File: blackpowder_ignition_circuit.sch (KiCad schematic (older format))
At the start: 6 parts, among them J2 Conn_01x02, Q1 FDS6898A

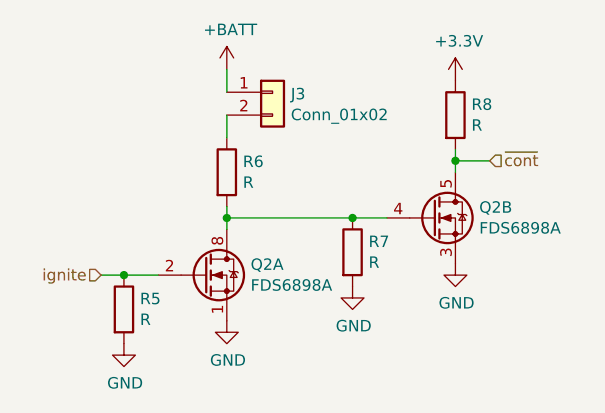
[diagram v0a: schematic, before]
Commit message: removed circuits that can't be fit in
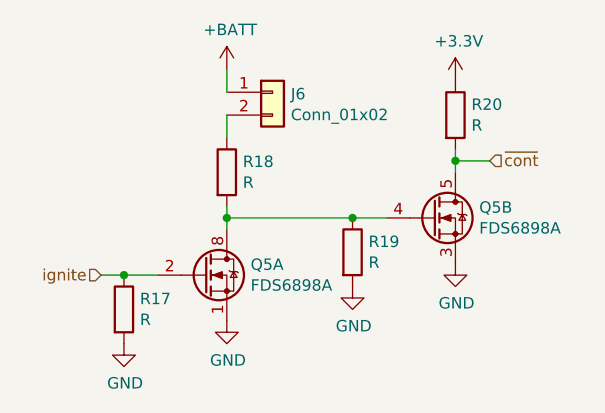
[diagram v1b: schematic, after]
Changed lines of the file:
@@
 $Descr A4 11693 8268
 encoding utf-8
-Sheet 2 8
+Sheet 5 6
 Title ""
 Date ""
@@
 AR Path="/5EB223EE/5EAFF725" Ref="Q7"  Part="1"
 AR Path="/5EB223F2/5EAFF725" Ref="Q8"  Part="1"
-F 0 "Q2" H 4404 4046 50  0000 L CNN
+F 0 "Q5" H 4404 4046 50  0000 L CNN
 F 1 "FDS6898A" H 4404 3955 50  0000 L CNN
 F 2 "Package_SO:SOIC-8_3.9x4.9mm_P1.27mm" H 4400 3925 50  0001 L CIN
@@
 AR Path="/5EB223EE/5EAFF72B" Ref="R25"  Part="1"
 AR Path="/5EB223F2/5EAFF72B" Ref="R29"  Part="1"
-F 0 "R5" H 3920 4196 50  0000 L CNN
+F 0 "R17" H 3920 4196 50  0000 L CNN
 F 1 "R" H 3920 4105 50  0000 L CNN
 F 2 "Resistor_SMD:R_0603_1608Metric_Pad1.05x0.95mm_HandSolder" V 3780 4150 50  0001 C CNN
@@
 AR Path="/5EB223EE/5EAFF731" Ref="R26"  Part="1"
 AR Path="/5EB223F2/5EAFF731" Ref="R30"  Part="1"
-F 0 "R6" H 4370 3596 50  0000 L CNN
+F 0 "R18" H 4370 3596 50  0000 L CNN
 F 1 "R" H 4370 3505 50  0000 L CNN
 F 2 "star-common-lib:PWR163" V 4230 3550 50  0001 C CNN
@@
 AR Path="/5EB223EE/5EAFF737" Ref="R27"  Part="1"
 AR Path="/5EB223F2/5EAFF737" Ref="R31"  Part="1"
-F 0 "R7" H 4920 3946 50  0000 L CNN
+F 0 "R19" H 4920 3946 50  0000 L CNN
 F 1 "R" H 4920 3855 50  0000 L CNN
 F 2 "Resistor_SMD:R_0603_1608Metric_Pad1.05x0.95mm_HandSolder" V 4780 3900 50  0001 C CNN
@@
 AR Path="/5EB223EE/5EAFF73D" Ref="Q7"  Part="2"
 AR Path="/5EB223F2/5EAFF73D" Ref="Q8"  Part="2"
-F 0 "Q2" H 5404 3796 50  0000 L CNN
+F 0 "Q5" H 5404 3796 50  0000 L CNN
 F 1 "FDS6898A" H 5404 3705 50  0000 L CNN
 F 2 "Package_SO:SOIC-8_3.9x4.9mm_P1.27mm" H 5400 3675 50  0001 L CIN
@@
 AR Path="/5EB223EE/5EAFF743" Ref="R28"  Part="1"
 AR Path="/5EB223F2/5EAFF743" Ref="R32"  Part="1"
-F 0 "R8" H 5370 3346 50  0000 L CNN
+F 0 "R20" H 5370 3346 50  0000 L CNN
 F 1 "R" H 5370 3255 50  0000 L CNN
 F 2 "Resistor_SMD:R_0603_1608Metric_Pad1.05x0.95mm_HandSolder" V 5230 3300 50  0001 C CNN
@@
 AR Path="/5EB223EE/5EAFF758" Ref="#PWR0137"  Part="1"
 AR Path="/5EB223F2/5EAFF758" Ref="#PWR0143"  Part="1"
-F 0 "#PWR0101" H 3850 4050 50  0001 C CNN
+F 0 "#PWR0125" H 3850 4050 50  0001 C CNN
 F 1 "GND" H 3855 4127 50  0000 C CNN
 F 2 "" H 3850 4300 50  0001 C CNN
@@
 AR Path="/5EB223EE/5EAFF75E" Ref="#PWR0138"  Part="1"
 AR Path="/5EB223F2/5EAFF75E" Ref="#PWR0144"  Part="1"
-F 0 "#PWR0102" H 4300 3950 50  0001 C CNN
+F 0 "#PWR0126" H 4300 3950 50  0001 C CNN
 F 1 "GND" H 4305 4027 50  0000 C CNN
 F 2 "" H 4300 4200 50  0001 C CNN
@@
 AR Path="/5EB223EE/5EAFF764" Ref="#PWR0139"  Part="1"
 AR Path="/5EB223F2/5EAFF764" Ref="#PWR0145"  Part="1"
-F 0 "#PWR0103" H 5300 3700 50  0001 C CNN
+F 0 "#PWR0127" H 5300 3700 50  0001 C CNN
 F 1 "GND" H 5305 3777 50  0000 C CNN
 F 2 "" H 5300 3950 50  0001 C CNN
@@
 AR Path="/5EB223EE/5EAFF76A" Ref="#PWR0140"  Part="1"
 AR Path="/5EB223F2/5EAFF76A" Ref="#PWR0146"  Part="1"
-F 0 "#PWR0104" H 4850 3800 50  0001 C CNN
+F 0 "#PWR0128" H 4850 3800 50  0001 C CNN
 F 1 "GND" H 4855 3877 50  0000 C CNN
 F 2 "" H 4850 4050 50  0001 C CNN
@@
 AR Path="/5EB223EE/5EAFF770" Ref="#PWR0141"  Part="1"
 AR Path="/5EB223F2/5EAFF770" Ref="#PWR0147"  Part="1"
-F 0 "#PWR0105" H 5300 3000 50  0001 C CNN
+F 0 "#PWR0129" H 5300 3000 50  0001 C CNN
 F 1 "+3.3V" H 5315 3323 50  0000 C CNN
 F 2 "" H 5300 3150 50  0001 C CNN
@@
 AR Path="/5EB223EE/5EAFF776" Ref="#PWR0142"  Part="1"
 AR Path="/5EB223F2/5EAFF776" Ref="#PWR0148"  Part="1"
-F 0 "#PWR0106" H 4300 2950 50  0001 C CNN
+F 0 "#PWR0130" H 4300 2950 50  0001 C CNN
 F 1 "+BATT" H 4315 3273 50  0000 C CNN
 F 2 "" H 4300 3100 50  0001 C CNN
@@
 AR Path="/5EB223EE/5EAFF77D" Ref="J8"  Part="1"
 AR Path="/5EB223F2/5EAFF77D" Ref="J9"  Part="1"
-F 0 "J3" H 4580 3192 50  0000 L CNN
+F 0 "J6" H 4580 3192 50  0000 L CNN
 F 1 "Conn_01x02" H 4580 3101 50  0000 L CNN
 F 2 "Connector_Molex:Molex_Mini-Fit_Jr_5569-02A2_2x01_P4.20mm_Horizontal" H 4500 3200 50  0001 C CNN

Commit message: everything hooked up, cleaned layout up, silkscreen
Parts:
- removed R2: R, star-common-lib:PWR163, symbol Device:R
- added J9: Conn_01x03, star-common-lib:PWR163, symbol Connector_Generic:Conn_01x03
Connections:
- wire segments 11 -> 12
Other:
- note added: "Resistor, pin 2 is heatsink"
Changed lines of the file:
@@
 $Descr A4 11693 8268
 encoding utf-8
-Sheet 5 6
+Sheet 5 5
 Title ""
 Date ""
@@
 AR Path="/5EB223EE/5EAFF725" Ref="Q7"  Part="1"
 AR Path="/5EB223F2/5EAFF725" Ref="Q8"  Part="1"
-F 0 "Q5" H 4404 4046 50  0000 L CNN
+F 0 "Q1" H 4404 4046 50  0000 L CNN
 F 1 "FDS6898A" H 4404 3955 50  0000 L CNN
 F 2 "Package_SO:SOIC-8_3.9x4.9mm_P1.27mm" H 4400 3925 50  0001 L CIN
@@
 AR Path="/5EB223EE/5EAFF72B" Ref="R25"  Part="1"
 AR Path="/5EB223F2/5EAFF72B" Ref="R29"  Part="1"
-F 0 "R17" H 3920 4196 50  0000 L CNN
+F 0 "R1" H 3920 4196 50  0000 L CNN
 F 1 "R" H 3920 4105 50  0000 L CNN
 F 2 "Resistor_SMD:R_0603_1608Metric_Pad1.05x0.95mm_HandSolder" V 3780 4150 50  0001 C CNN
 F 3 "~" H 3850 4150 50  0001 C CNN
 	1    3850 4150
-	1    0    0    -1
-$EndComp
-$Comp
-L Device:R R?
-U 1 1 5EAFF731
-P 4300 3550
-AR Path="/5EAFF731" Ref="R?"  Part="1"
-AR Path="/5EAF9C8B/5EAFF731" Ref="R2"  Part="1"
-AR Path="/5EB11141/5EAFF731" Ref="R?"  Part="1"
-AR Path="/5EB1278B/5EAFF731" Ref="R6"  Part="1"
-AR Path="/5EB12B7D/5EAFF731" Ref="R10"  Part="1"
-AR Path="/5EB12D6D/5EAFF731" Ref="R14"  Part="1"
-AR Path="/5EB1EA7C/5EAFF731" Ref="R18"  Part="1"
-AR Path="/5EB223E6/5EAFF731" Ref="R18"  Part="1"
-AR Path="/5EB223EA/5EAFF731" Ref="R22"  Part="1"
-AR Path="/5EB223EE/5EAFF731" Ref="R26"  Part="1"
-AR Path="/5EB223F2/5EAFF731" Ref="R30"  Part="1"
-F 0 "R18" H 4370 3596 50  0000 L CNN
-F 1 "R" H 4370 3505 50  0000 L CNN
-F 2 "star-common-lib:PWR163" V 4230 3550 50  0001 C CNN
-F 3 "~" H 4300 3550 50  0001 C CNN
-	1    4300 3550
 	1    0    0    -1
 $EndComp
@@
 AR Path="/5EB223EE/5EAFF737" Ref="R27"  Part="1"
 AR Path="/5EB223F2/5EAFF737" Ref="R31"  Part="1"
-F 0 "R19" H 4920 3946 50  0000 L CNN
+F 0 "R3" H 4920 3946 50  0000 L CNN
 F 1 "R" H 4920 3855 50  0000 L CNN
 F 2 "Resistor_SMD:R_0603_1608Metric_Pad1.05x0.95mm_HandSolder" V 4780 3900 50  0001 C CNN
@@
 AR Path="/5EB223EE/5EAFF73D" Ref="Q7"  Part="2"
 AR Path="/5EB223F2/5EAFF73D" Ref="Q8"  Part="2"
-F 0 "Q5" H 5404 3796 50  0000 L CNN
+F 0 "Q1" H 5404 3796 50  0000 L CNN
 F 1 "FDS6898A" H 5404 3705 50  0000 L CNN
 F 2 "Package_SO:SOIC-8_3.9x4.9mm_P1.27mm" H 5400 3675 50  0001 L CIN
@@
 AR Path="/5EB223EE/5EAFF743" Ref="R28"  Part="1"
 AR Path="/5EB223F2/5EAFF743" Ref="R32"  Part="1"
-F 0 "R20" H 5370 3346 50  0000 L CNN
+F 0 "R4" H 5370 3346 50  0000 L CNN
 F 1 "R" H 5370 3255 50  0000 L CNN
 F 2 "Resistor_SMD:R_0603_1608Metric_Pad1.05x0.95mm_HandSolder" V 5230 3300 50  0001 C CNN
@@
 Wire Wire Line
 	4850 3750 4300 3750
-Wire Wire Line
-	4300 3700 4300 3750
 Connection ~ 4850 3750
 Connection ~ 4300 3750
@@
 AR Path="/5EB223EE/5EAFF758" Ref="#PWR0137"  Part="1"
 AR Path="/5EB223F2/5EAFF758" Ref="#PWR0143"  Part="1"
-F 0 "#PWR0125" H 3850 4050 50  0001 C CNN
+F 0 "#PWR0101" H 3850 4050 50  0001 C CNN
 F 1 "GND" H 3855 4127 50  0000 C CNN
 F 2 "" H 3850 4300 50  0001 C CNN
@@
 AR Path="/5EB223EE/5EAFF75E" Ref="#PWR0138"  Part="1"
 AR Path="/5EB223F2/5EAFF75E" Ref="#PWR0144"  Part="1"
-F 0 "#PWR0126" H 4300 3950 50  0001 C CNN
+F 0 "#PWR0102" H 4300 3950 50  0001 C CNN
 F 1 "GND" H 4305 4027 50  0000 C CNN
 F 2 "" H 4300 4200 50  0001 C CNN
@@
 AR Path="/5EB223EE/5EAFF764" Ref="#PWR0139"  Part="1"
 AR Path="/5EB223F2/5EAFF764" Ref="#PWR0145"  Part="1"
-F 0 "#PWR0127" H 5300 3700 50  0001 C CNN
+F 0 "#PWR0103" H 5300 3700 50  0001 C CNN
 F 1 "GND" H 5305 3777 50  0000 C CNN
 F 2 "" H 5300 3950 50  0001 C CNN
@@
 AR Path="/5EB223EE/5EAFF76A" Ref="#PWR0140"  Part="1"
 AR Path="/5EB223F2/5EAFF76A" Ref="#PWR0146"  Part="1"
-F 0 "#PWR0128" H 4850 3800 50  0001 C CNN
+F 0 "#PWR0104" H 4850 3800 50  0001 C CNN
 F 1 "GND" H 4855 3877 50  0000 C CNN
 F 2 "" H 4850 4050 50  0001 C CNN
@@
 AR Path="/5EB223EE/5EAFF770" Ref="#PWR0141"  Part="1"
 AR Path="/5EB223F2/5EAFF770" Ref="#PWR0147"  Part="1"
-F 0 "#PWR0129" H 5300 3000 50  0001 C CNN
+F 0 "#PWR0105" H 5300 3000 50  0001 C CNN
 F 1 "+3.3V" H 5315 3323 50  0000 C CNN
 F 2 "" H 5300 3150 50  0001 C CNN
@@
 AR Path="/5EB223EE/5EAFF776" Ref="#PWR0142"  Part="1"
 AR Path="/5EB223F2/5EAFF776" Ref="#PWR0148"  Part="1"
-F 0 "#PWR0130" H 4300 2950 50  0001 C CNN
+F 0 "#PWR0106" H 4300 2950 50  0001 C CNN
 F 1 "+BATT" H 4315 3273 50  0000 C CNN
 F 2 "" H 4300 3100 50  0001 C CNN
@@
 	1    0    0    -1
 $EndComp
-Wire Wire Line
-	4300 3400 4300 3300
 $Comp
 L Connector_Generic:Conn_01x02 J?
@@
 AR Path="/5EB223EE/5EAFF77D" Ref="J8"  Part="1"
 AR Path="/5EB223F2/5EAFF77D" Ref="J9"  Part="1"
-F 0 "J6" H 4580 3192 50  0000 L CNN
+F 0 "J2" H 4580 3192 50  0000 L CNN
 F 1 "Conn_01x02" H 4580 3101 50  0000 L CNN
 F 2 "Connector_Molex:Molex_Mini-Fit_Jr_5569-02A2_2x01_P4.20mm_Horizontal" H 4500 3200 50  0001 C CNN
@@
 Text HLabel 5450 3500 2    50   Input ~ 0
 ~cont~
+$Comp
+L Connector_Generic:Conn_01x03 J9
+U 1 1 5EF99B5F
+P 4500 3550
+AR Path="/5EB12D6D/5EF99B5F" Ref="J9"  Part="1"
+AR Path="/5EB1278B/5EF99B5F" Ref="J6"  Part="1"
+AR Path="/5EB12B7D/5EF99B5F" Ref="J7"  Part="1"
+AR Path="/5EAF9C8B/5EF99B5F" Ref="J10"  Part="1"
+F 0 "J10" H 4580 3592 50  0000 L CNN
+F 1 "Conn_01x03" H 4580 3501 50  0000 L CNN
+F 2 "star-common-lib:PWR163" H 4500 3550 50  0001 C CNN
+F 3 "~" H 4500 3550 50  0001 C CNN
+	1    4500 3550
+	1    0    0    -1
+$EndComp
+Wire Wire Line
+	4300 3650 4300 3750
+Wire Wire Line
+	4300 3300 4300 3450
+$Comp
+L power:GND #PWR?
+U 1 1 5EF9AB74
+P 4100 3550
+AR Path="/5EF9AB74" Ref="#PWR?"  Part="1"
+AR Path="/5EAF9C8B/5EF9AB74" Ref="#PWR010"  Part="1"
+AR Path="/5EB11141/5EF9AB74" Ref="#PWR?"  Part="1"
+AR Path="/5EB1278B/5EF9AB74" Ref="#PWR07"  Part="1"
+AR Path="/5EB12B7D/5EF9AB74" Ref="#PWR08"  Part="1"
+AR Path="/5EB12D6D/5EF9AB74" Ref="#PWR09"  Part="1"
+AR Path="/5EB1EA7C/5EF9AB74" Ref="#PWR?"  Part="1"
+AR Path="/5EB223E6/5EF9AB74" Ref="#PWR?"  Part="1"
+AR Path="/5EB223EA/5EF9AB74" Ref="#PWR?"  Part="1"
+AR Path="/5EB223EE/5EF9AB74" Ref="#PWR?"  Part="1"
+AR Path="/5EB223F2/5EF9AB74" Ref="#PWR?"  Part="1"
+F 0 "#PWR010" H 4100 3300 50  0001 C CNN
+F 1 "GND" H 4105 3377 50  0000 C CNN
+F 2 "" H 4100 3550 50  0001 C CNN
+F 3 "" H 4100 3550 50  0001 C CNN
+	1    4100 3550
+	1    0    0    -1
+$EndComp
+Wire Wire Line
+	4100 3550 4300 3550
+Text Notes 2950 3550 0    50   ~ 0
+Resistor, pin 2 is heatsink
 $EndSCHEMATC

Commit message: most functionality
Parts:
- removed J9: Conn_01x03, star-common-lib:PWR163, symbol Connector_Generic:Conn_01x03
- added R6: 3R, star-common-lib:PWR163, symbol star-common-lib:R_Heatsink
- J2: footprint Connector_Molex:Molex_Mini-Fit_Jr_5569-02A2_2x01_P4.20mm_Horizontal -> star-common-lib:Molex_Mini-Fit_Jr_5569-02A2_2x01_P4.20mm_Horizontal
- R1, R3: value R -> 100k
- R4: value R -> 50k
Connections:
- wire segments 12 -> 10
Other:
- note removed: "Resistor, pin 2 is heatsink"
- moved on the sheet: R4
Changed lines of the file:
@@
 $Descr A4 11693 8268
 encoding utf-8
-Sheet 5 5
+Sheet 4 5
 Title ""
 Date ""
@@
 AR Path="/5EB223F2/5EAFF72B" Ref="R29"  Part="1"
 F 0 "R1" H 3920 4196 50  0000 L CNN
-F 1 "R" H 3920 4105 50  0000 L CNN
+F 1 "100k" H 3920 4105 50  0000 L CNN
 F 2 "Resistor_SMD:R_0603_1608Metric_Pad1.05x0.95mm_HandSolder" V 3780 4150 50  0001 C CNN
 F 3 "~" H 3850 4150 50  0001 C CNN
@@
 AR Path="/5EB223F2/5EAFF737" Ref="R31"  Part="1"
 F 0 "R3" H 4920 3946 50  0000 L CNN
-F 1 "R" H 4920 3855 50  0000 L CNN
+F 1 "100k" H 4920 3855 50  0000 L CNN
 F 2 "Resistor_SMD:R_0603_1608Metric_Pad1.05x0.95mm_HandSolder" V 4780 3900 50  0001 C CNN
 F 3 "~" H 4850 3900 50  0001 C CNN
@@
 L Device:R R?
 U 1 1 5EAFF743
-P 5300 3300
+P 5300 4150
 AR Path="/5EAFF743" Ref="R?"  Part="1"
 AR Path="/5EAF9C8B/5EAFF743" Ref="R4"  Part="1"
@@
 AR Path="/5EB223EE/5EAFF743" Ref="R28"  Part="1"
 AR Path="/5EB223F2/5EAFF743" Ref="R32"  Part="1"
-F 0 "R4" H 5370 3346 50  0000 L CNN
-F 1 "R" H 5370 3255 50  0000 L CNN
-F 2 "Resistor_SMD:R_0603_1608Metric_Pad1.05x0.95mm_HandSolder" V 5230 3300 50  0001 C CNN
-F 3 "~" H 5300 3300 50  0001 C CNN
-	1    5300 3300
+F 0 "R4" H 5370 4196 50  0000 L CNN
+F 1 "50k" H 5370 4105 50  0000 L CNN
+F 2 "Resistor_SMD:R_0603_1608Metric_Pad1.05x0.95mm_HandSolder" V 5230 4150 50  0001 C CNN
+F 3 "~" H 5300 4150 50  0001 C CNN
+	1    5300 4150
 	1    0    0    -1
 $EndComp
@@
 	4300 3750 4300 3800
 Wire Wire Line
-	5300 3450 5300 3500
-Wire Wire Line
 	3750 4000 3850 4000
 Connection ~ 3850 4000
-Wire Wire Line
-	5450 3500 5300 3500
-Connection ~ 5300 3500
-Wire Wire Line
-	5300 3500 5300 3550
 $Comp
 L power:GND #PWR?
@@
 L power:GND #PWR?
 U 1 1 5EAFF764
-P 5300 3950
+P 5300 4300
 AR Path="/5EAFF764" Ref="#PWR?"  Part="1"
 AR Path="/5EAF9C8B/5EAFF764" Ref="#PWR0103"  Part="1"
@@
 AR Path="/5EB223EE/5EAFF764" Ref="#PWR0139"  Part="1"
 AR Path="/5EB223F2/5EAFF764" Ref="#PWR0145"  Part="1"
-F 0 "#PWR0103" H 5300 3700 50  0001 C CNN
-F 1 "GND" H 5305 3777 50  0000 C CNN
-F 2 "" H 5300 3950 50  0001 C CNN
-F 3 "" H 5300 3950 50  0001 C CNN
-	1    5300 3950
+F 0 "#PWR0103" H 5300 4050 50  0001 C CNN
+F 1 "GND" H 5305 4127 50  0000 C CNN
+F 2 "" H 5300 4300 50  0001 C CNN
+F 3 "" H 5300 4300 50  0001 C CNN
+	1    5300 4300
 	1    0    0    -1
 $EndComp
@@
 L power:+3.3V #PWR?
 U 1 1 5EAFF770
-P 5300 3150
+P 5300 3550
 AR Path="/5EAFF770" Ref="#PWR?"  Part="1"
 AR Path="/5EAF9C8B/5EAFF770" Ref="#PWR0105"  Part="1"
@@
 AR Path="/5EB223EE/5EAFF770" Ref="#PWR0141"  Part="1"
 AR Path="/5EB223F2/5EAFF770" Ref="#PWR0147"  Part="1"
-F 0 "#PWR0105" H 5300 3000 50  0001 C CNN
-F 1 "+3.3V" H 5315 3323 50  0000 C CNN
-F 2 "" H 5300 3150 50  0001 C CNN
-F 3 "" H 5300 3150 50  0001 C CNN
-	1    5300 3150
+F 0 "#PWR0105" H 5300 3400 50  0001 C CNN
+F 1 "+3.3V" H 5315 3723 50  0000 C CNN
+F 2 "" H 5300 3550 50  0001 C CNN
+F 3 "" H 5300 3550 50  0001 C CNN
+	1    5300 3550
 	1    0    0    -1
 $EndComp
@@
 F 0 "J2" H 4580 3192 50  0000 L CNN
 F 1 "Conn_01x02" H 4580 3101 50  0000 L CNN
-F 2 "Connector_Molex:Molex_Mini-Fit_Jr_5569-02A2_2x01_P4.20mm_Horizontal" H 4500 3200 50  0001 C CNN
+F 2 "star-common-lib:Molex_Mini-Fit_Jr_5569-02A2_2x01_P4.20mm_Horizontal" H 4500 3200 50  0001 C CNN
 F 3 "~" H 4500 3200 50  0001 C CNN
 	1    4500 3200
@@
 Text HLabel 3750 4000 0    50   Input ~ 0
 ignite
-Text HLabel 5450 3500 2    50   Input ~ 0
+Text HLabel 5550 4000 2    50   Input ~ 0
 ~cont~
-$Comp
-L Connector_Generic:Conn_01x03 J9
-U 1 1 5EF99B5F
-P 4500 3550
-AR Path="/5EB12D6D/5EF99B5F" Ref="J9"  Part="1"
-AR Path="/5EB1278B/5EF99B5F" Ref="J6"  Part="1"
-AR Path="/5EB12B7D/5EF99B5F" Ref="J7"  Part="1"
-AR Path="/5EAF9C8B/5EF99B5F" Ref="J10"  Part="1"
-F 0 "J10" H 4580 3592 50  0000 L CNN
-F 1 "Conn_01x03" H 4580 3501 50  0000 L CNN
-F 2 "star-common-lib:PWR163" H 4500 3550 50  0001 C CNN
-F 3 "~" H 4500 3550 50  0001 C CNN
-	1    4500 3550
-	1    0    0    -1
-$EndComp
 Wire Wire Line
 	4300 3650 4300 3750
-Wire Wire Line
-	4300 3300 4300 3450
 $Comp
 L power:GND #PWR?
 U 1 1 5EF9AB74
-P 4100 3550
+P 4100 3500
 AR Path="/5EF9AB74" Ref="#PWR?"  Part="1"
 AR Path="/5EAF9C8B/5EF9AB74" Ref="#PWR010"  Part="1"
@@
 AR Path="/5EB223EE/5EF9AB74" Ref="#PWR?"  Part="1"
 AR Path="/5EB223F2/5EF9AB74" Ref="#PWR?"  Part="1"
-F 0 "#PWR010" H 4100 3300 50  0001 C CNN
-F 1 "GND" H 4105 3377 50  0000 C CNN
-F 2 "" H 4100 3550 50  0001 C CNN
-F 3 "" H 4100 3550 50  0001 C CNN
-	1    4100 3550
-	1    0    0    -1
-$EndComp
-Wire Wire Line
-	4100 3550 4300 3550
-Text Notes 2950 3550 0    50   ~ 0
-Resistor, pin 2 is heatsink
+F 0 "#PWR010" H 4100 3250 50  0001 C CNN
+F 1 "GND" H 4105 3327 50  0000 C CNN
+F 2 "" H 4100 3500 50  0001 C CNN
+F 3 "" H 4100 3500 50  0001 C CNN
+	1    4100 3500
+	1    0    0    -1
+$EndComp
+Wire Wire Line
+	5300 4000 5300 3950
+Wire Wire Line
+	5550 4000 5300 4000
+Connection ~ 5300 4000
+$Comp
+L star-common-lib:R_Heatsink R6
+U 1 1 5F271B62
+P 4300 3000
+AR Path="/5EB12B7D/5F271B62" Ref="R6"  Part="1"
+AR Path="/5EB12D6D/5F271B62" Ref="R10"  Part="1"
+AR Path="/5EB1278B/5F271B62" Ref="R2"  Part="1"
+AR Path="/5EAF9C8B/5F271B62" Ref="R14"  Part="1"
+F 0 "R14" H 4370 2546 50  0000 L CNN
+F 1 "3R" H 4370 2455 50  0000 L CNN
+F 2 "star-common-lib:PWR163" H 4300 3000 50  0001 C CNN
+F 3 "" H 4300 3000 50  0001 C CNN
+	1    4300 3000
+	1    0    0    -1
+$EndComp
+Wire Wire Line
+	4300 3350 4300 3300
 $EndSCHEMATC

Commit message: 8 charges on a module
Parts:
- removed R6: 3R, star-common-lib:PWR163, symbol star-common-lib:R_Heatsink
- added J3: Conn_01x02, star-common-lib:Molex_Mini-Fit_Jr_5569-02A2_2x01_P4.20mm_Horizontal, symbol Connector_Generic:Conn_01x02
- added unit 2 of Q1
- added Q2: FDS6898A, Package_SO:SOIC-8_3.9x4.9mm_P1.27mm, symbol Transistor_FET:FDS6898A
- added R2, R4: 100k, Resistor_SMD:R_0603_1608Metric_Pad0.98x0.95mm_HandSolder, symbol Device:R
- added R6: 50k, Resistor_SMD:R_0603_1608Metric_Pad0.98x0.95mm_HandSolder, symbol Device:R
- added U2: TC4427AVOA, Package_SO:MSOP-8-1EP_3x3mm_P0.65mm_EP2.5x3mm_Mask1.73x2.36mm, symbol eec:TC4427AVOA
- R1, R3, R4: footprint Resistor_SMD:R_0603_1608Metric_Pad1.05x0.95mm_HandSolder -> Resistor_SMD:R_0603_1608Metric_Pad0.98x0.95mm_HandSolder
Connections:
- net labels added: +5V, contA, contB, igniteA, igniteB
- net labels removed: ignite, ~cont~
- wire segments 10 -> 18
- no-connect marks 0 -> 2
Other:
- moved on the sheet: J9, Q7A, R19, R21, R23

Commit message: addressed review comments
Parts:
- removed Q1, Q2: FDS6898A, Package_SO:SOIC-8_3.9x4.9mm_P1.27mm, symbol Transistor_FET:FDS6898A
- added Q2: Q_DUAL_PMOS_S1G1D2S2G2D1, Package_TO_SOT_SMD:SOT-363_SC-70-6_Handsoldering, symbol Device:Q_DUAL_PMOS_S1G1D2S2G2D1
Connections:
- net +3V3: now also Q2.3 (D), Q2.6 (D)
- net at J2.2 (Pin_2), Q1.7 (D1), Q1.8 (D1)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: now also Q2.2 (G)
- net at J3.2 (Pin_2), Q1.5 (D2), Q1.6 (D2)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: now also Q2.5 (G)
- net contA renamed ~contA~
- net ~contA~: now also Q2.1 (S)
- net contB renamed ~contB~
- net ~contB~: now also Q2.4 (S)
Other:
- moved on the sheet: J10, J9, Q7A, Q7B, R19, R20, R21, R22, R23, R24, U5A, U5B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
